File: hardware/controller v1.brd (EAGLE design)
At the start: 100 x 80 mm, 11 parts, among them IC2 L293DD"

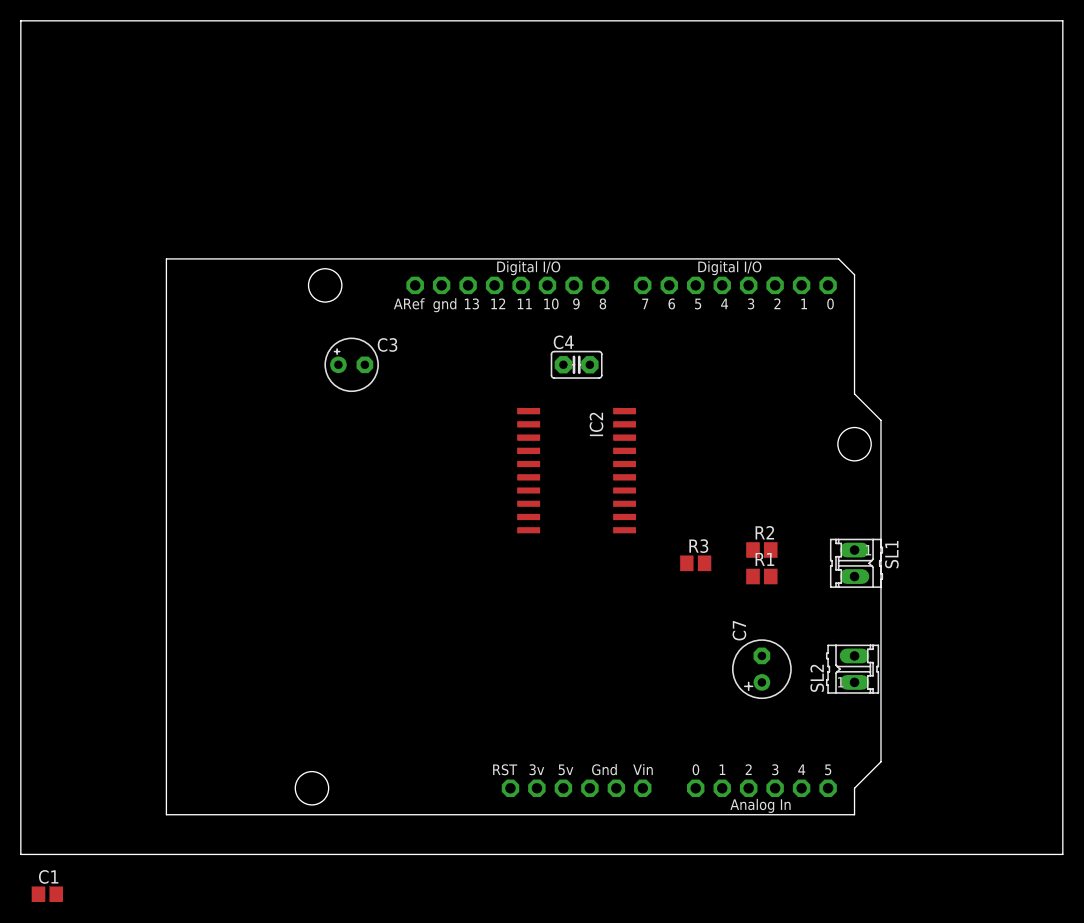
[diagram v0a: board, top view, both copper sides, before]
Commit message: Update on hardware schematics for Arduino shield
Final version will probably be a Beaglebone shield rather than Arduino,
but Arduino is so simple for testing...
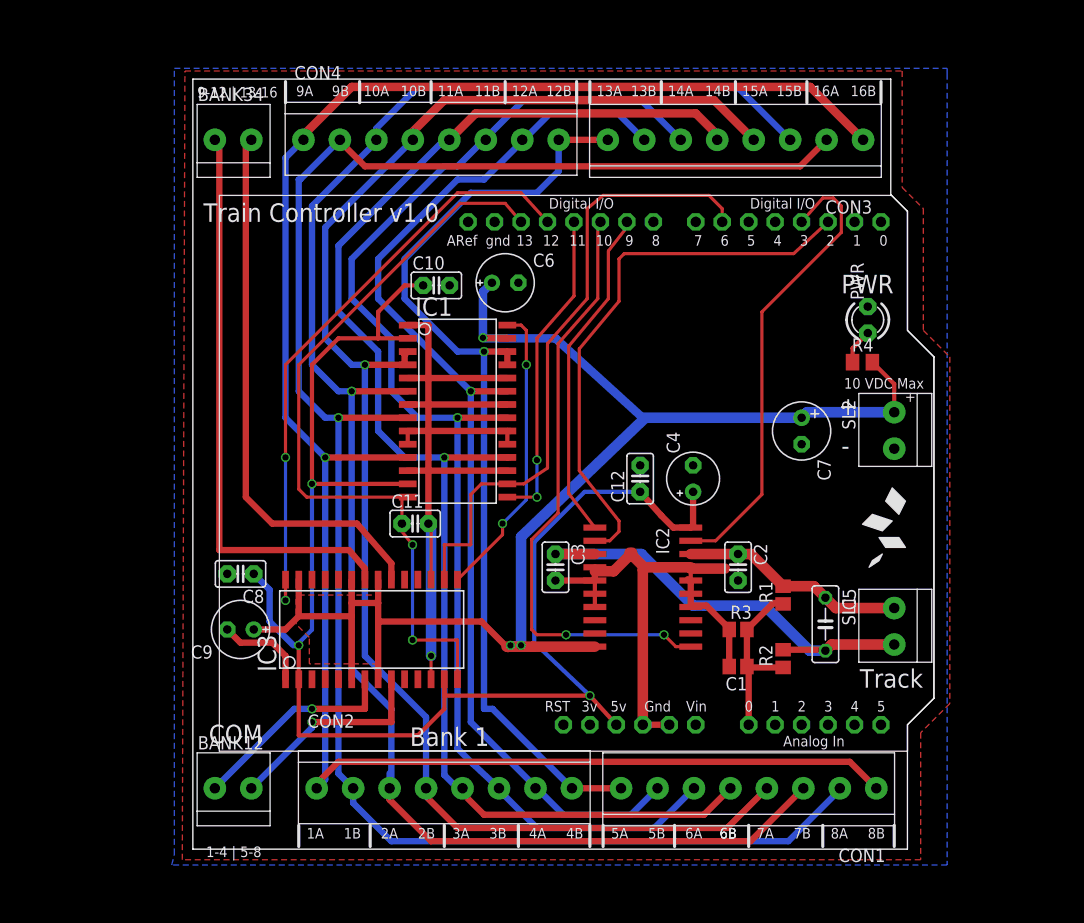
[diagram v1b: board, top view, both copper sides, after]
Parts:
- added BANK12, BANK34: 1X2-3.5MM, adafruit:1X2-3.5MM
- added C10, C11, C8: 0.1uF 6V, rcl-ez:C025-025X050
- added C12, C2: 0.1uF, rcl-ez:C025-025X050
- added C5: 330n, adafruit:C050-025X075
- added C6, C9: 10uF 20V, rcl:E2,5-6E
- added CON1, CON2, CON3, CON4: 1X08-CONN3.5MM, aerodynes:1X08-3.5MM
- added IC1, IC3: MC33880PEG, aerodynes:SO28W
- added PWR: (no value), minimidi:LED3MM
- added R4: 1.0K, rcl-ez:M0805
- added U$2: LOGO-AERODYNESSMALL, aerodynes:LOGO-AERODYNES-S
- C1: value (none) -> 220n
- C3: value 100uF/6V -> 0.1uF; device rcl-ez:E2,5-5 -> rcl-ez:C025-025X050
- C4: value 0.1uF -> 100uF/6V; device rcl-ez:C025-025X050 -> adafruit:E2,5-5
- IC2: value L293DD" -> L293DD
- R1, R2, R3: value (none) -> 10k
- SL1, SL2: value (none) -> 1X2-3.5MM; device con-amp-quick:02P -> adafruit:1X2-3.5MM
- U$1: value ARDUINOUNO -> ARDUINO; device adafruit:ARDUINO -> aerodynes:ARDUINO-NOCUT
- moved C1 69.8 mm to (68.8, 18.0), turned to 180 degrees
- moved U$1 44.8 mm to (30.5, 45.5)
- moved C3 27.6 mm to (51.3, 27.6), turned to 270 degrees
- moved C7 23.2 mm to (74.9, 40.6), turned to 270 degrees
- moved SL2 23.2 mm to (83.8, 40.6)
- moved C4 15.6 mm to (64.5, 36.1), turned to 90 degrees
- moved IC2 12.9 mm to (59.7, 25.7)
- moved R2 10.6 mm to (73.2, 18.8), turned to 90 degrees
- moved R3 7.54 mm to (68.8, 21.6)
- moved SL1 7.19 mm to (83.8, 21.8), turned to 90 degrees
- moved R1 2.70 mm to (73.2, 24.9), turned to 90 degrees
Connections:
- removed net GND1: U$1.GND1
- removed net GND2: IC2.5
- removed net GND3: IC2.6
- removed net GND6: IC2.15
- removed net GND7: IC2.16
- new net CS: IC1.16, IC3.16, U$1.D6
- new net DEBUG: U$1.D7
- new net MISO: IC3.28, U$1.D12
- new net MOSI: IC1.15, U$1.D11
- new net N$1: BANK12.2, IC3.7
- new net N$11: CON1.1, CON2.1, CON3.1, CON4.1, IC1.25, IC1.26
- new net N$12: CON1.8, CON2.8, CON3.8, CON4.8, IC1.11
- new net N$13: IC1.28, IC3.15
- new net N$14: CON1.7, CON2.7, CON3.7, CON4.7, IC1.8
- new net N$15: CON1.2, CON2.2, CON3.2, CON4.2, IC1.23
- new net N$16: CON1.6, CON2.6, CON3.6, CON4.6, IC1.6
- new net N$2: BANK12.1, IC3.9
- new net N$3: BANK34.1, IC3.20
- new net N$35: PWR.A, R4.1
- new net N$4: BANK34.2, IC3.22
- new net N$7: CON1.3, CON2.3, CON3.3, CON4.3, IC1.21
- new net N$8: CON1.4, CON2.4, CON3.4, CON4.4, IC1.18
- new net N$9: CON1.5, CON2.5, CON3.5, CON4.5, IC1.3, IC1.4
- new net SCLK: C11.1, IC1.14, IC3.14, U$1.D13
- net 1Y: now also C3.1, C5.2, R2.2; no longer R1.2
- net 4Y: now also C2.1, C5.1, R1.2; no longer R2.2
- net GND: now also C10.2, C11.2, C12.2, C2.2, C3.2, C4.-, C6.-, C8.2, C9.-, IC1.1, IC1.10, IC1.12, IC1.17, IC1.19, IC1.20, IC1.22, IC1.24, IC1.5, IC1.7, IC1.9, IC2.12, IC2.15, IC2.16, IC2.5, IC2.6, IC2.9, IC3.1, IC3.12, IC3.17, PWR.K, U$1.GND1; no longer C3.-, C4.2
- net V+: now also C6.+, C9.+, IC1.27, IC3.21, IC3.23, IC3.27, IC3.6, IC3.8, R4.2
- net VCC: now also C10.1, C12.1, C4.+, C8.1, IC1.13, IC1.2, IC3.13, IC3.2; no longer C3.+, C4.1
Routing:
- net N$12: track 0.00 -> 187.0 mm, vias 0 -> 1
- net N$14: track 0.00 -> 174.4 mm, vias 0 -> 1
- net N$16: track 0.00 -> 164.8 mm, vias 0 -> 1
- net VCC: track 0.00 -> 148.7 mm, vias 0 -> 3
- net N$9: track 0.00 -> 148.6 mm, vias 0 -> 1
- net GND: track 0.00 -> 146.3 mm, vias 0 -> 1
- net V+: track 0.00 -> 145.4 mm, vias 0 -> 3
- net N$8: track 0.00 -> 136.9 mm, vias 0 -> 1
- net N$7: track 0.00 -> 125.3 mm, vias 0 -> 1
- net N$15: track 0.00 -> 106.9 mm, vias 0 -> 1
- net N$11: track 0.00 -> 93.6 mm, vias 0 -> 1
- net SCLK: track 0.00 -> 73.4 mm, vias 0 -> 2
- net CS: track 0.00 -> 60.5 mm
- net PWM2: track 0.00 -> 57.8 mm, vias 0 -> 2
- net MISO: track 0.00 -> 57.8 mm, vias 0 -> 2
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- added copper zone on layer 1, net GND
- added copper zone on layer 16, net GND
- added copper zone on layer 1, net V+
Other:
- board size 100 x 80 mm -> 71.1 x 73.9 mm
- board text added: "+"
- board text added: "-"
- board text added: "1-4 | 5-8"
- board text added: "10 VDC Max"
- board text added: "10A"
- board text added: "10B"
- board text added: "11A"
- board text added: "11B"
- board text added: "12A"
- board text added: "12B"
- board text added: "13A"
- board text added: "13B"
- board text added: "14A"
- board text added: "14B"
- board text added: "15A"
- board text added: "15B"
- board text added: "16A"
- board text added: "16B"
- board text added: "1A"
- board text added: "1B"
- board text added: "2A"
- board text added: "2B"
- board text added: "3A"
- board text added: "3B"
- board text added: "4A"
- board text added: "4B"
- board text added: "5A"
- board text added: "5B"
- board text added: "6A"
- board text added: "6B"
- board text added: "7A"
- board text added: "7B"
- board text added: "8A"
- board text added: "8B"
- board text added: "9-12 | 13-16"
- board text added: "9A"
- board text added: "9B"
- board text added: "Bank 1"
- board text added: "COM"
- board text added: "PWR"
- board text added: "Track"
- board text added: "Train Controller v1.0"

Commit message: Big bugfix on hardware controller schematics and board.
The 33880 pinout was reversed on my schematics...
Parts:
- added C13: (no value), resistor:C0805K
- added R5: 50m, resistor:M1206
- added R6: 10k, resistor:R0603
- added R7: (no value), resistor:R0603
- added U$3: ZXCT1009-F, aerodynes:SOT23-1TOP
- moved C1 3.18 mm to (68.8, 21.2)
- moved C2 2.55 mm to (69.1, 30.1), turned to 90 degrees
- moved R3 2.29 mm to (68.8, 23.9)
- moved R2 1.14 mm to (73.2, 19.9), turned to 270 degrees
- moved R1 0.25 mm to (73.2, 24.6)
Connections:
- new net CURR_MEASURE: C13.1, R7.1, U$1.A1
- new net N$5: IC2.10, R5.2, U$3.3
- new net N$6: R6.2, R7.2, U$3.1
- net 1A: now also U$1.D3; no longer U$1.D2
- net 4A: now also U$1.D2; no longer U$1.D3
- net GND: now also C13.2, IC1.11, IC1.18, IC1.21, IC1.23, IC1.25, IC1.26, IC1.3, IC1.4, IC1.6, IC1.8, R6.1; no longer IC1.10, IC1.19, IC1.20, IC1.22, IC1.24, IC1.5, IC1.7, IC1.9
- net N$1: now also BANK34.2, IC3.23; no longer BANK12.2, IC3.7
- net N$11: now also IC1.24; no longer IC1.25, IC1.26
- net N$12: now also IC1.10; no longer IC1.11
- net N$14: now also IC1.9; no longer IC1.8
- net N$15: now also IC1.22; no longer IC1.23
- net N$16: now also IC1.7; no longer IC1.6
- net N$2: now also BANK34.1, IC3.21; no longer BANK12.1, IC3.9
- net N$3: now also BANK12.1, IC3.6; no longer BANK34.1, IC3.20
- net N$4: now also BANK12.2, IC3.8; no longer BANK34.2, IC3.22
- net N$7: now also IC1.20; no longer IC1.21
- net N$8: now also IC1.19; no longer IC1.18
- net N$9: now also IC1.5; no longer IC1.3, IC1.4
- net V+: now also IC3.20, IC3.22, IC3.7, IC3.9, R5.1, U$3.2; no longer IC2.10, IC3.21, IC3.23, IC3.6, IC3.8
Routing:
- net GND: track 146.3 -> 60.4 mm
- net N$1: track 20.4 -> 51.8 mm, vias 1 -> 0
- net N$2: track 20.5 -> 50.8 mm, vias 1 -> 0
- net N$3: track 52.8 -> 22.9 mm
- net N$4: track 55.4 -> 29.3 mm
- net CURR_MEASURE: track 0.00 -> 13.2 mm
- net VCC: track 148.7 -> 160.7 mm
- net 4A: track 44.7 -> 54.9 mm
- net N$5: track 0.00 -> 9.39 mm
- net V+: track 145.4 -> 150.4 mm
- net N$6: track 0.00 -> 4.65 mm
- net N$11: track 93.6 -> 90.9 mm
- net N$9: track 148.6 -> 146.5 mm
- net 1A: track 53.0 -> 50.9 mm
- net PWM2: track 57.8 -> 56.3 mm
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- removed copper zone on layer 1, net V+
